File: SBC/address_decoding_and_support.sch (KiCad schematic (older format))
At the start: 14 parts, among them SW1 RESET, U5 TL7705B, U7 ispMACH4A5, U8 74HC74, X1 8 MHz

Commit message: Preparation for Pluto v3.0
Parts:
- removed C21, C22: 0.1uF, Capacitors_ThroughHole:C_Disc_D4.7mm_W2.5mm_P5.00mm, symbol device:C_Small
- removed RN1, RN2: 3.3 kOhm, Resistors_THT:R_Array_SIP8, symbol device:R_Network07
- removed U7: ispMACH4A5, Package_LCC:PLCC-44_THT-Socket, symbol pluto:ispMACH4A5
- added C9: 0.1uF, Capacitor_THT:C_Disc_D4.7mm_W2.5mm_P5.00mm, symbol Device:C_Small
- added Q1: DS1813, Package_TO_SOT_THT:TO-92L_Inline, symbol Device:Q_NPN_CBE
- added RN1: 3.3k, Resistor_THT:R_Array_SIP9, symbol Device:R_Network08
- added SW2: PANIC, Button_Switch_THT:SW_PUSH_6mm_H4.3mm, symbol pluto-rescue:SW_Push-switches
- added U6: PlutoDecoder, Package_DIP:DIP-24_W7.62mm_Socket, symbol Grotto:PlutoDecoder
- C4: footprint Capacitors_ThroughHole:CP_Radial_Tantal_D4.5mm_P2.50mm -> Capacitor_THT:CP_Radial_Tantal_D4.5mm_P2.50mm; symbol device:CP_Small -> pluto-rescue:CP_Small-device
- C6: footprint Capacitors_ThroughHole:C_Disc_D4.7mm_W2.5mm_P5.00mm -> Capacitor_THT:C_Disc_D4.7mm_W2.5mm_P5.00mm; symbol device:C_Small -> pluto-rescue:C_Small-device
- R2, R3, R4: footprint Resistors_ThroughHole:R_Axial_DIN0411_L9.9mm_D3.6mm_P7.62mm_Vertical -> Resistor_THT:R_Axial_DIN0411_L9.9mm_D3.6mm_P7.62mm_Vertical; symbol device:R_Small -> pluto-rescue:R_Small-device
- SW1: footprint Buttons_Switches_ThroughHole:SW_PUSH_6mm_h4.3mm -> Button_Switch_THT:SW_PUSH_6mm_H4.3mm; symbol switches:SW_Push -> pluto-rescue:SW_Push-switches
- U5: footprint Housings_DIP:DIP-8_W7.62mm_Socket -> Package_DIP:DIP-8_W7.62mm_Socket
- U8: footprint Housings_DIP:DIP-14_W7.62mm_Socket -> Package_DIP:DIP-14_W7.62mm_Socket
- X1: footprint Oscillators:Oscillator_DIP-8 -> Oscillator:Oscillator_DIP-8; symbol Oscillators:CXO_DIP8 -> pluto-rescue:CXO_DIP8-Oscillators
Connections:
- net labels added: R-~W, ~DUART, ~IO, ~RTC, ~VIA1SEL, ~VIA2SEL
- net labels removed: A3, DIOR, DIOW, FROM_CLK, FROM_OE, IDE_CS0, OBT_DIR, OBT_OE, R/~W, TCK, TDI, TDO, TMS, TO_CLK, TO_OE, ~7F8X, ~7FAX, ~7FCX, ~7FEX
- wire segments 121 -> 90
- no-connect marks 8 -> 3

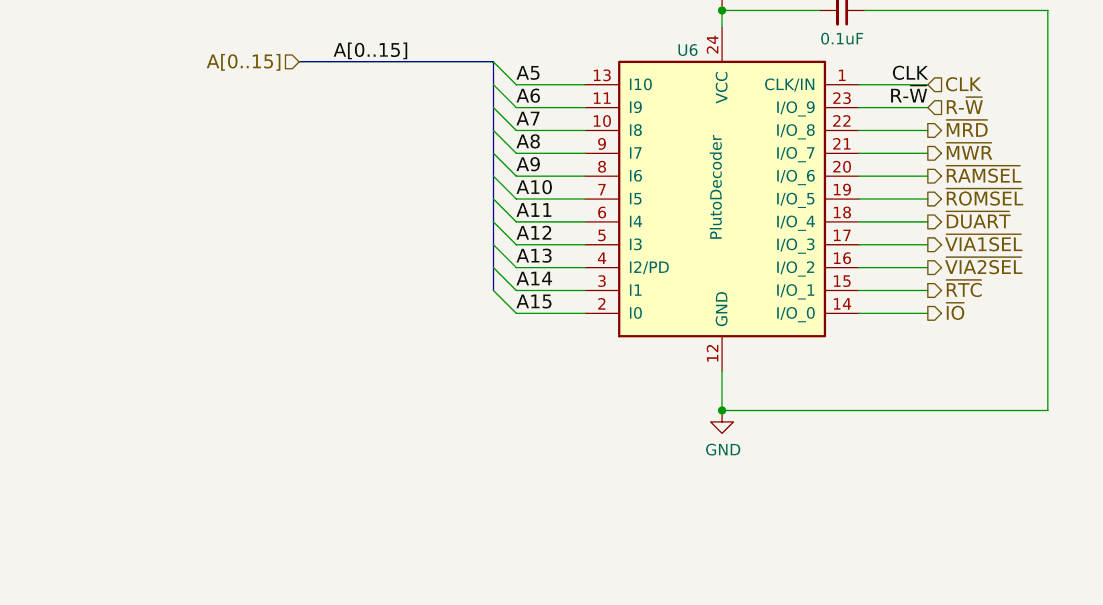
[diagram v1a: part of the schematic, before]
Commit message: A better layout of PCB.
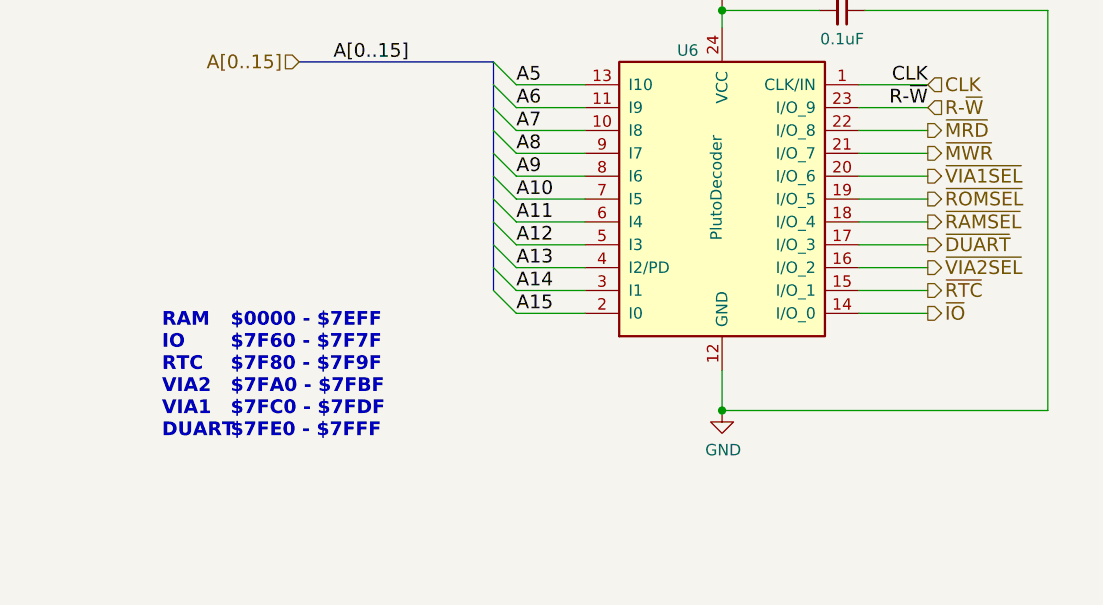
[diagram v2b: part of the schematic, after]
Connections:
- net ~DUART: now also U6.17 (I/O_3); no longer U6.18 (I/O_4)
- net ~RAMSEL: now also U6.18 (I/O_4); no longer U6.20 (I/O_6)
- net ~VIA1SEL: now also U6.20 (I/O_6); no longer U6.17 (I/O_3)
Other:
- note added: "$0000 - $7EFF\n$7F60 - $7F7F\n$7F80 - $7F9F\n$7FA0 - $7FBF\n$7FC0 - $7FDF\n$7FE0 - $7FFF"
- note added: "RAM\nIO \nRTC\nVIA2\nVIA1\nDUART"
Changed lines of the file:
@@
 Text HLabel 9275 1425 2    60   Output ~ 0
 ~MWR
-Text HLabel 9275 1525 2    60   Output ~ 0
+Text HLabel 9275 1725 2    60   Output ~ 0
 ~RAMSEL
 Text HLabel 9275 1625 2    60   Output ~ 0
 ~ROMSEL
-Text HLabel 9275 1725 2    60   Output ~ 0
+Text HLabel 9275 1825 2    60   Output ~ 0
 ~DUART
-Text HLabel 9275 1825 2    60   Output ~ 0
+Text HLabel 9275 1525 2    60   Output ~ 0
 ~VIA1SEL
 Text HLabel 9275 1925 2    60   Output ~ 0
@@
 Wire Bus Line
 	7375 1025 7375 2025
+Text Notes 5925 2675 0    60   ~ 12
+RAM\nIO \nRTC\nVIA2\nVIA1\nDUART
+Text Notes 6225 2675 0    60   ~ 12
+$0000 - $7EFF\n$7F60 - $7F7F\n$7F80 - $7F9F\n$7FA0 - $7FBF\n$7FC0 - $7FDF\n$7FE0 - $7FFF
 $EndSCHEMATC

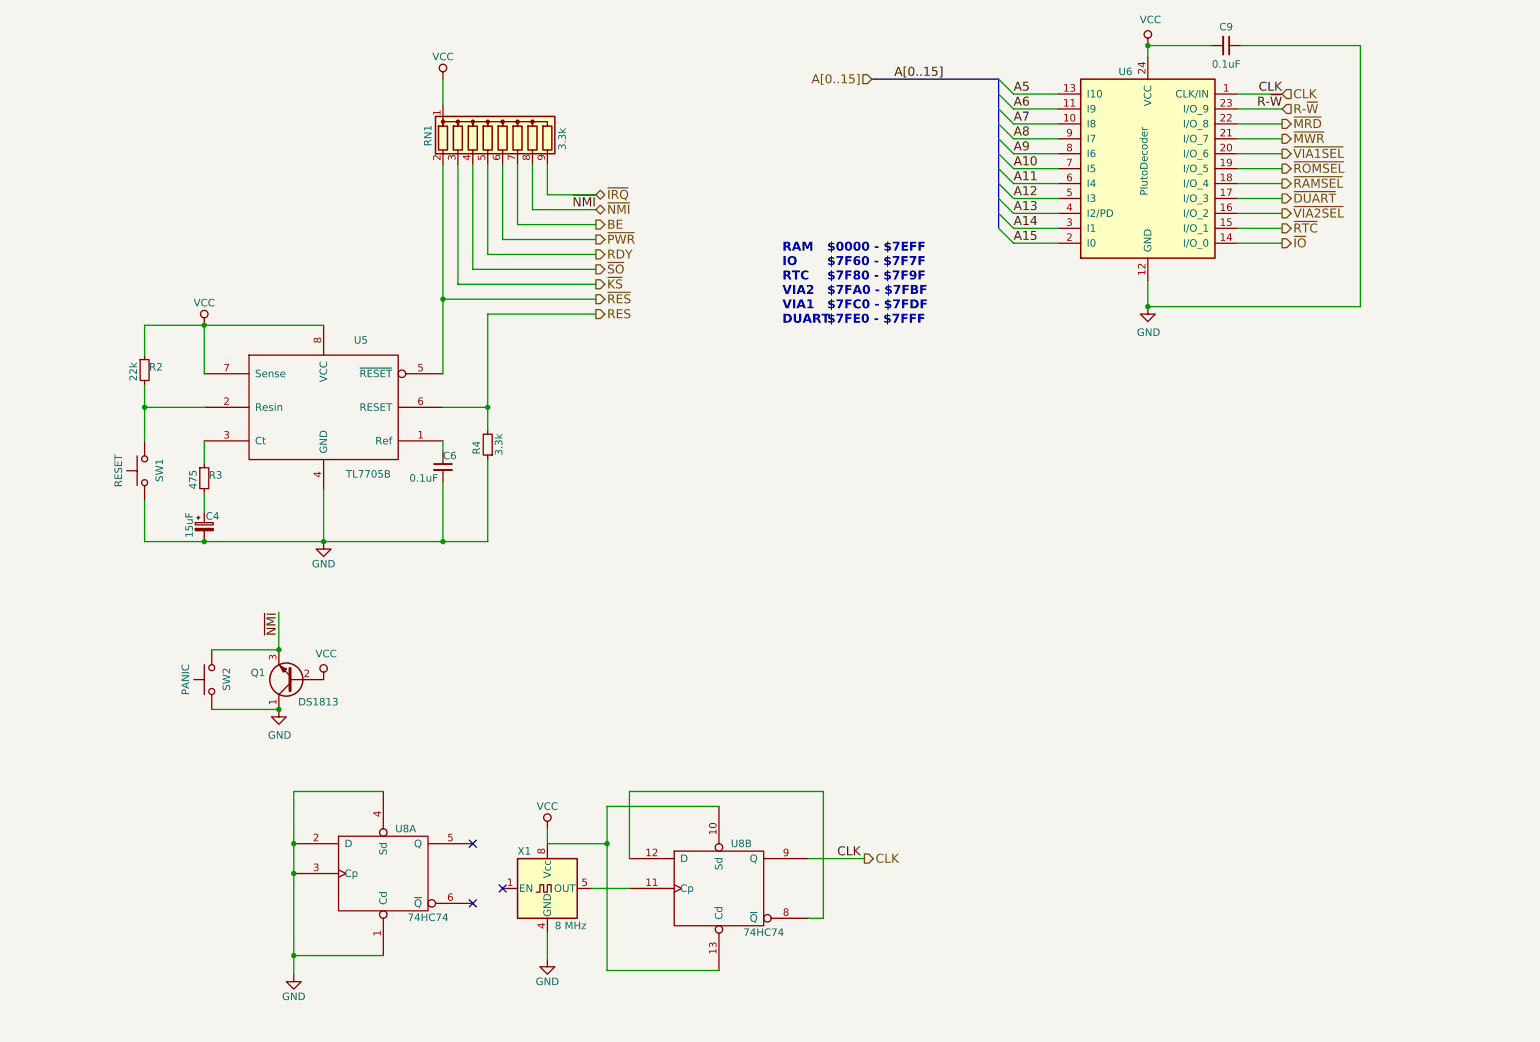
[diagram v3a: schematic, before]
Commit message: Converting to SMD of almost all components.
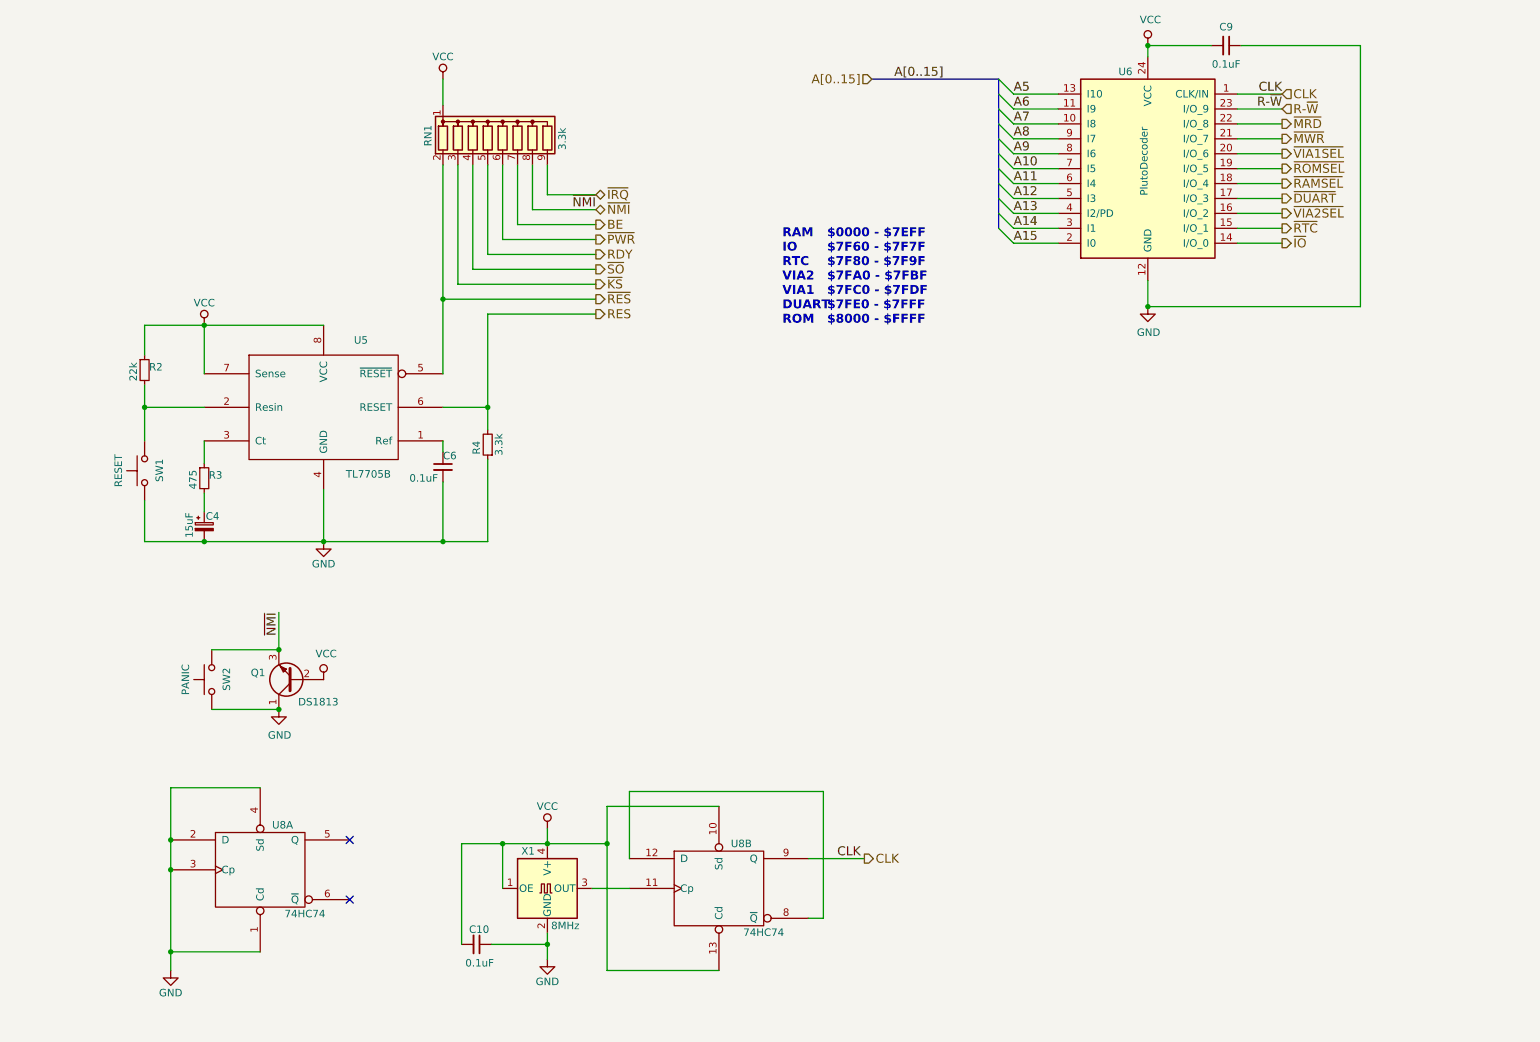
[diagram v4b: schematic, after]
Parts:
- removed X1: 8 MHz, Oscillator:Oscillator_DIP-8, symbol pluto-rescue:CXO_DIP8-Oscillators
- added C10: 0.1uF, Capacitor_SMD:C_0603_1608Metric_Pad1.05x0.95mm_HandSolder, symbol pluto-rescue:C_Small-device
- added X1: 8MHz, Oscillator:Oscillator_SMD_SeikoEpson_SG8002CA-4Pin_7.0x5.0mm, symbol Oscillator:SG-8002CA
- C4: footprint Capacitor_THT:CP_Radial_Tantal_D4.5mm_P2.50mm -> Capacitor_Tantalum_SMD:CP_EIA-7343-31_Kemet-D_Pad2.25x2.55mm_HandSolder
- C6, C9: footprint Capacitor_THT:C_Disc_D4.7mm_W2.5mm_P5.00mm -> Capacitor_SMD:C_0603_1608Metric_Pad1.05x0.95mm_HandSolder
- Q1: footprint Package_TO_SOT_THT:TO-92L_Inline -> Package_TO_SOT_SMD:SOT-23_Handsoldering
- R2, R3, R4: footprint Resistor_THT:R_Axial_DIN0411_L9.9mm_D3.6mm_P7.62mm_Vertical -> Resistor_SMD:R_1206_3216Metric_Pad1.42x1.75mm_HandSolder
- RN1: footprint Resistor_THT:R_Array_SIP9 -> Resistor_SMD:R_Array_Convex_8x0602
- U5: footprint Package_DIP:DIP-8_W7.62mm_Socket -> Package_SO:SOIC-8_3.9x4.9mm_P1.27mm
- U8: footprint Package_DIP:DIP-14_W7.62mm_Socket -> Package_SO:SOIC-14_3.9x8.7mm_P1.27mm
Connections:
- net GND: now also C10.1, X1.2 (GND)
- net VCC: now also C10.2, X1.1 (OE), X1.4 (V+)
- net at U8.11 (Cp): now also X1.3 (OUT)
- no-connect marks 3 -> 2
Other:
- note added: "$0000 - $7EFF\n$7F60 - $7F7F\n$7F80 - $7F9F\n$7FA0 - $7FBF\n$7FC0 - $7FDF\n$7FE0 - $7FFF\n$8000 - $FFFF"
- note added: "RAM\nIO \nRTC\nVIA2\nVIA1\nDUART\nROM"
- note removed: "$0000 - $7EFF\n$7F60 - $7F7F\n$7F80 - $7F9F\n$7FA0 - $7FBF\n$7FC0 - $7FDF\n$7FE0 - $7FFF"
- note removed: "RAM\nIO \nRTC\nVIA2\nVIA1\nDUART"
- moved on the sheet: U8A
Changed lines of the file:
@@
 Rev "0.1"
 Comp "Linux Grotto"
-Comment1 "The decoding logic is a slightly modied version of Daryl Rictor's SBC-2 v2.5"
-Comment2 ""
-Comment3 ""
-Comment4 ""
+Comment1 "Decoding logic in an ATF22V10 GAL"
+Comment2 "Pullups for various signals"
+Comment3 "Clock generator"
+Comment4 "Reset and NMI logic."
 $EndDescr
-$Comp
-L pluto-rescue:CXO_DIP8-Oscillators X1
-U 1 1 58D6C921
-P 4350 6450
-F 0 "X1" H 4150 6700 50  0000 L CNN
-F 1 "8 MHz" H 4400 6200 50  0000 L CNN
-F 2 "Oscillator:Oscillator_DIP-8" H 4800 6100 50  0001 C CNN
-F 3 "" H 4250 6450 50  0001 C CNN
-	1    4350 6450
-	1    0    0    -1
-$EndComp
 $Comp
 L power:VCC #PWR09
@@
 L power:GND #PWR015
 U 1 1 595DE156
-P 2650 7025
-F 0 "#PWR015" H 2650 6775 50  0001 C CNN
-F 1 "GND" H 2650 6875 50  0000 C CNN
-F 2 "" H 2650 7025 50  0001 C CNN
-F 3 "" H 2650 7025 50  0001 C CNN
-	1    2650 7025
-	1    0    0    -1
-$EndComp
-NoConn ~ 3850 6150
-NoConn ~ 3850 6550
-NoConn ~ 4050 6450
+P 1825 7000
+F 0 "#PWR015" H 1825 6750 50  0001 C CNN
+F 1 "GND" H 1825 6850 50  0000 C CNN
+F 2 "" H 1825 7000 50  0001 C CNN
+F 3 "" H 1825 7000 50  0001 C CNN
+	1    1825 7000
+	1    0    0    -1
+$EndComp
+NoConn ~ 3025 6125
+NoConn ~ 3025 6525
 $Comp
 L pluto-rescue:74HC74 U8
@@
 F 0 "U8" H 5650 6750 50  0000 C CNN
 F 1 "74HC74" H 5800 6155 50  0000 C CNN
-F 2 "Package_DIP:DIP-14_W7.62mm_Socket" H 5500 6450 50  0001 C CNN
+F 2 "Package_SO:SOIC-14_3.9x8.7mm_P1.27mm" H 5500 6450 50  0001 C CNN
 F 3 "" H 5500 6450 50  0001 C CNN
 	2    5500 6450
@@
 L pluto-rescue:74HC74 U8
 U 1 1 59EC7994
-P 3250 6350
-F 0 "U8" H 3400 6650 50  0000 C CNN
-F 1 "74HC74" H 3550 6055 50  0000 C CNN
-F 2 "Package_DIP:DIP-14_W7.62mm_Socket" H 3250 6350 50  0001 C CNN
-F 3 "" H 3250 6350 50  0001 C CNN
-	1    3250 6350
+P 2425 6325
+F 0 "U8" H 2575 6625 50  0000 C CNN
+F 1 "74HC74" H 2725 6030 50  0000 C CNN
+F 2 "Package_SO:SOIC-14_3.9x8.7mm_P1.27mm" H 2425 6325 50  0001 C CNN
+F 3 "" H 2425 6325 50  0001 C CNN
+	1    2425 6325
 	1    0    0    -1
 $EndComp
@@
 F 0 "U5" H 3100 3675 50  0000 C CNN
 F 1 "TL7705B" H 3150 2777 50  0000 C CNN
-F 2 "Package_DIP:DIP-8_W7.62mm_Socket" H 2850 3225 50  0001 C CNN
+F 2 "Package_SO:SOIC-8_3.9x4.9mm_P1.27mm" H 2850 3225 50  0001 C CNN
 F 3 "" H 2850 3225 50  0001 C CNN
 	1    2850 3225
@@
 F 0 "R2" H 1680 2995 50  0000 L CNN
 F 1 "22k" V 1575 2900 50  0000 L CNN
-F 2 "Resistor_THT:R_Axial_DIN0411_L9.9mm_D3.6mm_P7.62mm_Vertical" H 1650 2975 50  0001 C CNN
+F 2 "Resistor_SMD:R_1206_3216Metric_Pad1.42x1.75mm_HandSolder" H 1650 2975 50  0001 C CNN
 F 3 "" H 1650 2975 50  0001 C CNN
 	1    1650 2975
@@
 F 0 "R3" H 2080 3720 50  0000 L CNN
 F 1 "475" V 1975 3625 50  0000 L CNN
-F 2 "Resistor_THT:R_Axial_DIN0411_L9.9mm_D3.6mm_P7.62mm_Vertical" H 2050 3700 50  0001 C CNN
+F 2 "Resistor_SMD:R_1206_3216Metric_Pad1.42x1.75mm_HandSolder" H 2050 3700 50  0001 C CNN
 F 3 "" H 2050 3700 50  0001 C CNN
 	1    2050 3700
@@
 F 0 "C4" H 2060 4095 50  0000 L CNN
 F 1 "15uF" V 1950 3950 50  0000 L CNN
-F 2 "Capacitor_THT:CP_Radial_Tantal_D4.5mm_P2.50mm" H 2050 4025 50  0001 C CNN
+F 2 "Capacitor_Tantalum_SMD:CP_EIA-7343-31_Kemet-D_Pad2.25x2.55mm_HandSolder" H 2050 4025 50  0001 C CNN
 F 3 "" H 2050 4025 50  0001 C CNN
 	1    2050 4025
@@
 F 0 "C6" H 3650 3700 50  0000 L CNN
 F 1 "0.1uF" H 3425 3550 50  0000 L CNN
-F 2 "Capacitor_THT:C_Disc_D4.7mm_W2.5mm_P5.00mm" H 3650 3625 50  0001 C CNN
+F 2 "Capacitor_SMD:C_0603_1608Metric_Pad1.05x0.95mm_HandSolder" H 3650 3625 50  0001 C CNN
 F 3 "" H 3650 3625 50  0001 C CNN
 	1    3650 3625
@@
 F 0 "R4" V 4025 3450 50  0000 L CNN
 F 1 "3.3k" V 3875 3400 50  0000 L CNN
-F 2 "Resistor_THT:R_Axial_DIN0411_L9.9mm_D3.6mm_P7.62mm_Vertical" H 3950 3475 50  0001 C CNN
+F 2 "Resistor_SMD:R_1206_3216Metric_Pad1.42x1.75mm_HandSolder" H 3950 3475 50  0001 C CNN
 F 3 "" H 3950 3475 50  0001 C CNN
 	1    3950 3475
@@
 	4650 6450 4900 6450
 Wire Wire Line
-	4350 6750 4350 6925
+	4350 6750 4350 6825
 Wire Wire Line
 	4350 6150 4350 6050
@@
 	6100 6250 6475 6250
 Wire Wire Line
-	3250 5800 2650 5800
-Wire Wire Line
-	2650 5800 2650 6150
-Connection ~ 2650 6150
-Connection ~ 2650 6350
-Wire Wire Line
-	3250 6900 2650 6900
-Connection ~ 2650 6900
+	2425 5775 1825 5775
+Wire Wire Line
+	1825 5775 1825 6125
+Connection ~ 1825 6125
+Connection ~ 1825 6325
+Wire Wire Line
+	2425 6875 1825 6875
+Connection ~ 1825 6875
 Wire Wire Line
 	2050 3000 2050 2675
@@
 	4750 6150 4750 7000
 Wire Wire Line
-	2650 6150 2650 6350
-Wire Wire Line
-	2650 6350 2650 6900
-Wire Wire Line
-	2650 6900 2650 7025
+	1825 6125 1825 6325
+Wire Wire Line
+	1825 6325 1825 6875
+Wire Wire Line
+	1825 6875 1825 7000
 Wire Wire Line
 	2050 4125 2850 4125
@@
 F 0 "RN1" V 3550 1325 50  0000 L CNN
 F 1 "3.3k" V 4450 1300 50  0000 L CNN
-F 2 "Resistor_THT:R_Array_SIP9" V 4525 1400 50  0001 C CNN
+F 2 "Resistor_SMD:R_Array_Convex_8x0602" V 4525 1400 50  0001 C CNN
 F 3 "http://www.vishay.com/docs/31509/csc.pdf" H 4050 1400 50  0001 C CNN
 	1    4050 1400
@@
 F 0 "Q1" H 2841 5004 50  0000 L CNN
 F 1 "DS1813" H 2350 5200 50  0000 L CNN
-F 2 "Package_TO_SOT_THT:TO-92L_Inline" H 2850 5150 50  0001 C CNN
+F 2 "Package_TO_SOT_SMD:SOT-23_Handsoldering" H 2850 5150 50  0001 C CNN
 F 3 "~" H 2650 5050 50  0001 C CNN
 	1    2650 5050
@@
 F 0 "C9" V 8775 800 50  0000 C CNN
 F 1 "0.1uF" V 9025 800 50  0000 C CNN
-F 2 "Capacitor_THT:C_Disc_D4.7mm_W2.5mm_P5.00mm" H 8900 800 50  0001 C CNN
+F 2 "Capacitor_SMD:C_0603_1608Metric_Pad1.05x0.95mm_HandSolder" H 8900 800 50  0001 C CNN
 F 3 "~" H 8900 800 50  0001 C CNN
 	1    8900 800
@@
 Connection ~ 8375 2550
 Text Notes 5925 2675 0    60   ~ 12
-RAM\nIO \nRTC\nVIA2\nVIA1\nDUART
+RAM\nIO \nRTC\nVIA2\nVIA1\nDUART\nROM
 Text Notes 6225 2675 0    60   ~ 12
-$0000 - $7EFF\n$7F60 - $7F7F\n$7F80 - $7F9F\n$7FA0 - $7FBF\n$7FC0 - $7FDF\n$7FE0 - $7FFF
+$0000 - $7EFF\n$7F60 - $7F7F\n$7F80 - $7F9F\n$7FA0 - $7FBF\n$7FC0 - $7FDF\n$7FE0 - $7FFF\n$8000 - $FFFF
+$Comp
+L Oscillator:SG-8002CA X1
+U 1 1 5D6922F2
+P 4350 6450
+F 0 "X1" H 4175 6700 50  0000 L CNN
+F 1 "8MHz" H 4375 6200 50  0000 L CNN
+F 2 "Oscillator:Oscillator_SMD_SeikoEpson_SG8002CA-4Pin_7.0x5.0mm" H 5050 6100 50  0001 C CNN
+F 3 "https://support.epson.biz/td/api/doc_check.php?mode=dl&lang=en&Parts=SG-8002DC" H 4250 6450 50  0001 C CNN
+	1    4350 6450
+	1    0    0    -1
+$EndComp
+Connection ~ 4350 6150
+Wire Wire Line
+	4050 6450 4050 6150
+Wire Wire Line
+	4050 6150 4350 6150
+$Comp
+L pluto-rescue:C_Small-device C10
+U 1 1 5D69CF17
+P 3875 6825
+F 0 "C10" V 3775 6775 50  0000 L CNN
+F 1 "0.1uF" V 4000 6750 50  0000 L CNN
+F 2 "Capacitor_SMD:C_0603_1608Metric_Pad1.05x0.95mm_HandSolder" H 3875 6825 50  0001 C CNN
+F 3 "" H 3875 6825 50  0001 C CNN
+	1    3875 6825
+	0    1    1    0
+$EndComp
+Wire Wire Line
+	3975 6825 4350 6825
+Connection ~ 4350 6825
+Wire Wire Line
+	4350 6825 4350 6925
+Wire Wire Line
+	3775 6825 3775 6150
+Wire Wire Line
+	3775 6150 4050 6150
+Connection ~ 4050 6150
 Wire Bus Line
 	7375 1025 7375 2025
